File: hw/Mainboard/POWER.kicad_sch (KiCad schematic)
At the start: 36 parts, among them J10 5V PWR, J11 3V3 PWR, J18 PET_Power_01x09_Male, J7 9V POWER, U10 XL1509-5.0E1, U15 LM317AG-TN3-R

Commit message: hw: wip add MCU, 2 layer board
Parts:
- removed D8: YLW LED, LED_SMD:LED_0603_1608Metric, symbol Device:LED
- removed D9: GRN LED, LED_SMD:LED_0603_1608Metric, symbol Device:LED
- removed J11: 3V3 PWR, Connector_PinHeader_2.54mm:PinHeader_1x03_P2.54mm_Vertical, symbol Connector:Conn_01x03_Male
- removed R48: 1.5k, Resistor_SMD:R_0402_1005Metric, symbol Device:R_Small
- removed R51: 1k, Resistor_SMD:R_0402_1005Metric, symbol Device:R_Small
- added C21: 22u 25V, Capacitor_SMD:C_0805_2012Metric, symbol Device:C_Small
- added C34: 10uF 50V, Capacitor_SMD:C_1206_3216Metric, symbol Device:C_Small
- added C36: 22u, Capacitor_SMD:C_0805_2012Metric, symbol Device:C_Small
- added H3, H4: MountingHole, PET:PET_MountingHole_4mm, symbol Mechanical:MountingHole
- added U13: AMS1117-3.3, Package_TO_SOT_SMD:SOT-223-3_TabPin2, symbol Regulator_Linear:AMS1117-3.3
- C29: value 1u -> 1u 25V
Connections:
- net +3V3: now also C36.1, U13.2 (VO)
- net +5V: now also C21.1, C34.1, U13.3 (VI)
- net GND: now also C21.2, C34.2, C36.2, U13.1 (GND)
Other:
- moved on the sheet: C14, C16, C22, C26, C29, C32, H1, H2, R42, R43, R45, R46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

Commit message: hw: T8 (wip)
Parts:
- added C52, C53: 22u 25V, Capacitor_SMD:C_0805_2012Metric, symbol Device:C_Small
- added C54, C55: 10u, Capacitor_Tantalum_SMD:CP_EIA-3216-18_Kemet-A, symbol T8Dev-rescue:CP-Device
- added C56, C57: 100n, Capacitor_SMD:C_0402_1005Metric, symbol Device:C_Small
- added C58: 4.7u, Capacitor_SMD:C_0402_1005Metric, symbol Device:C_Small
- added FB1: 600, Inductor_SMD:L_0603_1608Metric, symbol T8Dev-rescue:Ferrite_Bead_Small-Device
- added U17: LM1117-1.2, Package_TO_SOT_SMD:SOT-223, symbol Regulator_Linear:LM1117-3.3
- added U21: T8Q144C3, SnapEDA:QFP50P2200X2200X160-144N, symbol SnapEDA:T8Q144C3
- J18: value PET_Power_01x09_Male -> PET POWER
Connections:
- net +3V3: now also C54.1, U17.3 (VI), U21.12 (VCCIO1C_1D), U21.122 (VCCIO3A), U21.143 (VCCIO1E), U21.21 (VCCIO1B), U21.23 (VCCIO1A), U21.51 (VCCIO4B), U21.52 (VCCIO4B), U21.62 (VCCIO4A), U21.63 (VCCIO4A), U21.88 (VCCIO3E), U21.91 (VCCIO3D), U21.95 (VCCIO3B_3C)
- net +9V_Unreg: now also C52.1, C53.1; no longer C13.1
- net GND: now also C52.2, C53.2, C54.2, C55.2, C56.2, C57.2, C58.2, U17.1 (GND), U21.1 (GND), U21.104 (GND), U21.108 (GND), U21.120 (GND), U21.121 (GND), U21.126 (GND), U21.127 (GND), U21.129 (GND), U21.133 (GND), U21.37 (GND), U21.44 (GND), U21.5 (GND), U21.50 (GND), U21.64 (GND), U21.9 (GND), U21.94 (GND)
- net at C12.2, C15.1, C33.2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: now also C13.1
- new net: C57.1, C58.1, FB1.1, U21.107 (VCCA_TR), U21.2 (VCCA_TL), U21.73 (VCCA_BR)
- new net VCORE: C55.1, C56.1, FB1.2, U17.2 (VO), U21.125 (VCC), U21.128 (VCC), U21.13 (VCC), U21.130 (VCC), U21.22 (VCC), U21.49 (VCC), U21.57 (VCC), U21.85 (VCC), U21.96 (VCC)
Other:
- note added: "Dropout Voltage = 1.3V"
- note added: "T8Q144 Power Requirements Absolute max VCORE: 1.42V Typical: 1.15V ~ 1.25V"
- note added: "VCCA is the analog VCORE source for PLLs"
- moved on the sheet: C12, C13, C14, C15, C16, C17, C21, C22, C26, C29, C32, C33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

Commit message: hw: routing (excluding MCU)
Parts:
- added J11: 9V POWER, Connector_PinHeader_2.54mm:PinHeader_1x02_P2.54mm_Vertical, symbol Connector:Conn_01x02_Male
- C36: value 22u -> 22u 25V
- C54, C55: value 10u -> 10u 16V
- D1: value RED LED -> RED_9V
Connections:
- net +9V_Unreg: now also J11.2 (Pin_2)
- net GND: now also J11.1 (Pin_1)
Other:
- note added: "AMS1117-3.3: Dropout Voltage = 1.3V"
- note added: "T8Q144 Power Requirements Absolute max VCORE: 1.42V Typical: 1.15V ~ 1.25V LM1117-12: VOUT = 1.176V - 1.224V (IOUT = 10ma, VIN = 3.5V) VOUT = 1.152V - 1.248V (10mA <= IOUT <= 1A, 3.0 <= VIN <= 10V) VIN = 12V (max recommended) Dropout Voltage = 1.2V @ 1A"
- note removed: "Dropout Voltage = 1.3V"
- note removed: "T8Q144 Power Requirements Absolute max VCORE: 1.42V Typical: 1.15V ~ 1.25V"
- moved on the sheet: C55
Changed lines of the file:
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@@
   (junction (at 242.57 144.78) (diameter 0) (color 0 0 0 0)
   )
+  (junction (at 54.61 38.1) (diameter 0) (color 0 0 0 0)
+  )
   (junction (at 109.22 106.68) (diameter 0) (color 0 0 0 0)
   )
@@
   (junction (at 147.32 49.53) (diameter 0) (color 0 0 0 0)
   )
+  (junction (at 45.72 43.18) (diameter 0) (color 0 0 0 0)
+  )
   (junction (at 109.22 68.58) (diameter 0) (color 0 0 0 0)
   )
@@
   (junction (at 172.72 49.53) (diameter 0) (color 0 0 0 0)
   )
-  (junction (at 142.24 135.89) (diameter 0) (color 0 0 0 0)
-  )
   (junction (at 186.69 49.53) (diameter 0) (color 0 0 0 0)
   )
@@
   )
   (junction (at 242.57 119.38) (diameter 0) (color 0 0 0 0)
+  )
+  (junction (at 144.78 135.89) (diameter 0) (color 0 0 0 0)
   )
   (junction (at 241.3 111.76) (diameter 0) (color 0 0 0 0)
@@
     (stroke (width 0) (type default) (color 0 0 0 0))
   )
-  (wire (pts (xy 142.24 144.78) (xy 128.27 144.78))
+  (wire (pts (xy 128.27 144.78) (xy 144.78 144.78))
     (stroke (width 0) (type default) (color 0 0 0 0))
   )
@@
     (stroke (width 0) (type default) (color 0 0 0 0))
   )
+  (wire (pts (xy 54.61 38.1) (xy 67.31 38.1))
+    (stroke (width 0) (type default) (color 0 0 0 0))
+  )
   (wire (pts (xy 39.37 40.64) (xy 39.37 43.18))
     (stroke (width 0) (type default) (color 0 0 0 0))
@@
     (stroke (width 0) (type default) (color 0 0 0 0))
   )
-  (wire (pts (xy 142.24 135.89) (xy 157.48 135.89))
+  (wire (pts (xy 135.89 135.89) (xy 144.78 135.89))
     (stroke (width 0) (type default) (color 0 0 0 0))
   )
@@
     (stroke (width 0) (type default) (color 0 0 0 0))
   )
+  (wire (pts (xy 45.72 43.18) (xy 67.31 43.18))
+    (stroke (width 0) (type default) (color 0 0 0 0))
+  )
   (wire (pts (xy 243.84 119.38) (xy 242.57 119.38))
     (stroke (width 0) (type default) (color 0 0 0 0))
@@
     (stroke (width 0) (type default) (color 0 0 0 0))
   )
-  (wire (pts (xy 142.24 143.51) (xy 142.24 144.78))
+  (wire (pts (xy 144.78 143.51) (xy 144.78 144.78))
     (stroke (width 0) (type default) (color 0 0 0 0))
   )
@@
     (stroke (width 0) (type default) (color 0 0 0 0))
   )
-  (wire (pts (xy 135.89 135.89) (xy 142.24 135.89))
-    (stroke (width 0) (type default) (color 0 0 0 0))
-  )
   (wire (pts (xy 259.08 31.75) (xy 255.27 31.75))
     (stroke (width 0) (type default) (color 0 0 0 0))
@@
     (stroke (width 0) (type default) (color 0 0 0 0))
   )
+  (wire (pts (xy 144.78 135.89) (xy 157.48 135.89))
+    (stroke (width 0) (type default) (color 0 0 0 0))
+  )
   (wire (pts (xy 246.38 50.8) (xy 247.65 50.8))
     (stroke (width 0) (type default) (color 0 0 0 0))
@@
     (stroke (width 0) (type default) (color 0 0 0 0))
   )
+  (wire (pts (xy 67.31 40.64) (xy 67.31 43.18))
+    (stroke (width 0) (type default) (color 0 0 0 0))
+  )
   (wire (pts (xy 27.94 93.98) (xy 36.83 93.98))
     (stroke (width 0) (type default) (color 0 0 0 0))
@@
     (stroke (width 0) (type default) (color 0 0 0 0))
   )
-  (text "T8Q144 Power Requirements\n\nAbsolute max VCORE: 1.42V\nTypical: 1.15V ~ 1.25V"
-    (at 134.62 156.21 0)
+  (text "T8Q144 Power Requirements\nAbsolute max VCORE: 1.42V\nTypical: 1.15V ~ 1.25V\n\nLM1117-12:\nVOUT = 1.176V - 1.224V (IOUT = 10ma, VIN = 3.5V)\nVOUT = 1.152V - 1.248V (10mA <= IOUT <= 1A, 3.0 <= VIN <= 10V)\nVIN = 12V (max recommended)\nDropout Voltage = 1.2V @ 1A"
+    (at 166.37 146.05 0)
     (effects (font (size 1.27 1.27)) (justify left bottom))
   )
   (text "In the PET, pins 2 and 4 are connected externally with a\n23000u capacitor to reduce ripple in the rectified 9V.\n\nOlder 2001 PETs had a 5 pin connector, which was expanded\nto 9 pins in a compatible way.  Pin 7 is key.  Pins 8/9\nare an additional AC input for generating +16V and +12V.\n\nRAW power connectors shown in the original PET schematics\nprovide unregulated +16V/-9V power to internal accessories,\nsuch as RAM expanders.\n\nThe PET monitor gets power directly from the transformer.\n"
-    (at 22.86 144.78 0)
+    (at 20.32 147.32 0)
     (effects (font (size 1.27 1.27)) (justify left bottom))
   )
@@
     (effects (font (size 1.27 1.27)) (justify left bottom))
   )
-  (text "Dropout Voltage = 1.3V" (at 135.89 120.65 0)
+  (text "AMS1117-3.3:\nDropout Voltage = 1.3V" (at 138.43 123.19 0)
     (effects (font (size 1.27 1.27)) (justify left bottom))
   )
@@
     (in_bom yes) (on_board yes)
     (property "Reference" "D1" (id 0) (at 263.0678 25.273 0))
-    (property "Value" "RED LED" (id 1) (at 263.0678 27.5844 0))
+    (property "Value" "RED_9V" (id 1) (at 263.0678 27.5844 0))
     (property "Footprint" "LED_SMD:LED_0603_1608Metric" (id 2) (at 262.89 31.75 0)
       (effects (font (size 1.27 1.27)) hide)
@@
     )
     (pin "1")
+  )
+  (symbol (lib_id "Connector:Conn_01x02_Male") (at 72.39 40.64 180) (unit 1)
+    (in_bom yes) (on_board yes) (fields_autoplaced)
+    (property "Reference" "J11" (id 0) (at 73.66 38.0999 0)
+      (effects (font (size 1.27 1.27)) (justify right))
+    )
+    (property "Value" "9V POWER" (id 1) (at 73.66 40.6399 0)
+      (effects (font (size 1.27 1.27)) (justify right))
+    )
+    (property "Footprint" "Connector_PinHeader_2.54mm:PinHeader_1x02_P2.54mm_Vertical" (id 2) (at 72.39 40.64 0)
+      (effects (font (size 1.27 1.27)) hide)
+    )
+    (property "Datasheet" "~" (id 3) (at 72.39 40.64 0)
+      (effects (font (size 1.27 1.27)) hide)
+    )
+    (pin "1")
+    (pin "2")
   )
   (symbol (lib_id "SnapEDA:T8Q144C3") (at 259.08 127 0) (unit 13)
@@
       (effects (font (size 1.27 1.27)) (justify left))
     )
-    (property "Value" "22u" (id 1) (at 147.32 111.7662 0)
+    (property "Value" "22u 25V" (id 1) (at 147.32 111.7662 0)
       (effects (font (size 1.27 1.27)) (justify left))
     )
@@
       (effects (font (size 1.27 1.27)) (justify left))
     )
-    (property "Value" "10u" (id 1) (at 112.2172 140.843 0)
+    (property "Value" "10u 16V" (id 1) (at 112.2172 140.843 0)
       (effects (font (size 1.27 1.27)) (justify left))
     )
@@
     (pin "1")
   )
-  (symbol (lib_id "T8Dev-rescue:CP-Device") (at 142.24 139.7 0) (unit 1)
-    (in_bom yes) (on_board yes)
-    (property "Reference" "C55" (id 0) (at 145.2372 138.5316 0)
-      (effects (font (size 1.27 1.27)) (justify left))
-    )
-    (property "Value" "10u" (id 1) (at 145.2372 140.843 0)
-      (effects (font (size 1.27 1.27)) (justify left))
-    )
-    (property "Footprint" "Capacitor_Tantalum_SMD:CP_EIA-3216-18_Kemet-A" (id 2) (at 143.2052 143.51 0)
-      (effects (font (size 1.27 1.27)) hide)
-    )
-    (property "Datasheet" "https://datasheet.lcsc.com/lcsc/1811071223_AVX-TAJA106K016RNJ_C7171.pdf" (id 3) (at 142.24 139.7 0)
-      (effects (font (size 1.27 1.27)) hide)
-    )
-    (property "LCSC" "C7171" (id 4) (at 142.24 139.7 0)
-      (effects (font (size 1.27 1.27)) hide)
-    )
+  (symbol (lib_id "T8Dev-rescue:CP-Device") (at 144.78 139.7 0) (unit 1)
+    (in_bom yes) (on_board yes)
+    (property "Reference" "C55" (id 0) (at 147.7772 138.5316 0)
+      (effects (font (size 1.27 1.27)) (justify left))
+    )
+    (property "Value" "10u 16V" (id 1) (at 147.7772 140.843 0)
+      (effects (font (size 1.27 1.27)) (justify left))
+    )
+    (property "Footprint" "Capacitor_Tantalum_SMD:CP_EIA-3216-18_Kemet-A" (id 2) (at 145.7452 143.51 0)
+      (effects (font (size 1.27 1.27)) hide)
+    )
+    (property "Datasheet" "https://datasheet.lcsc.com/lcsc/1811071223_AVX-TAJA106K016RNJ_C7171.pdf" (id 3) (at 144.78 139.7 0)
+      (effects (font (size 1.27 1.27)) hide)
+    )
+    (property "LCSC" "C7171" (id 4) (at 144.78 139.7 0)
+      (effects (font (size 1.27 1.27)) hide)
+    )

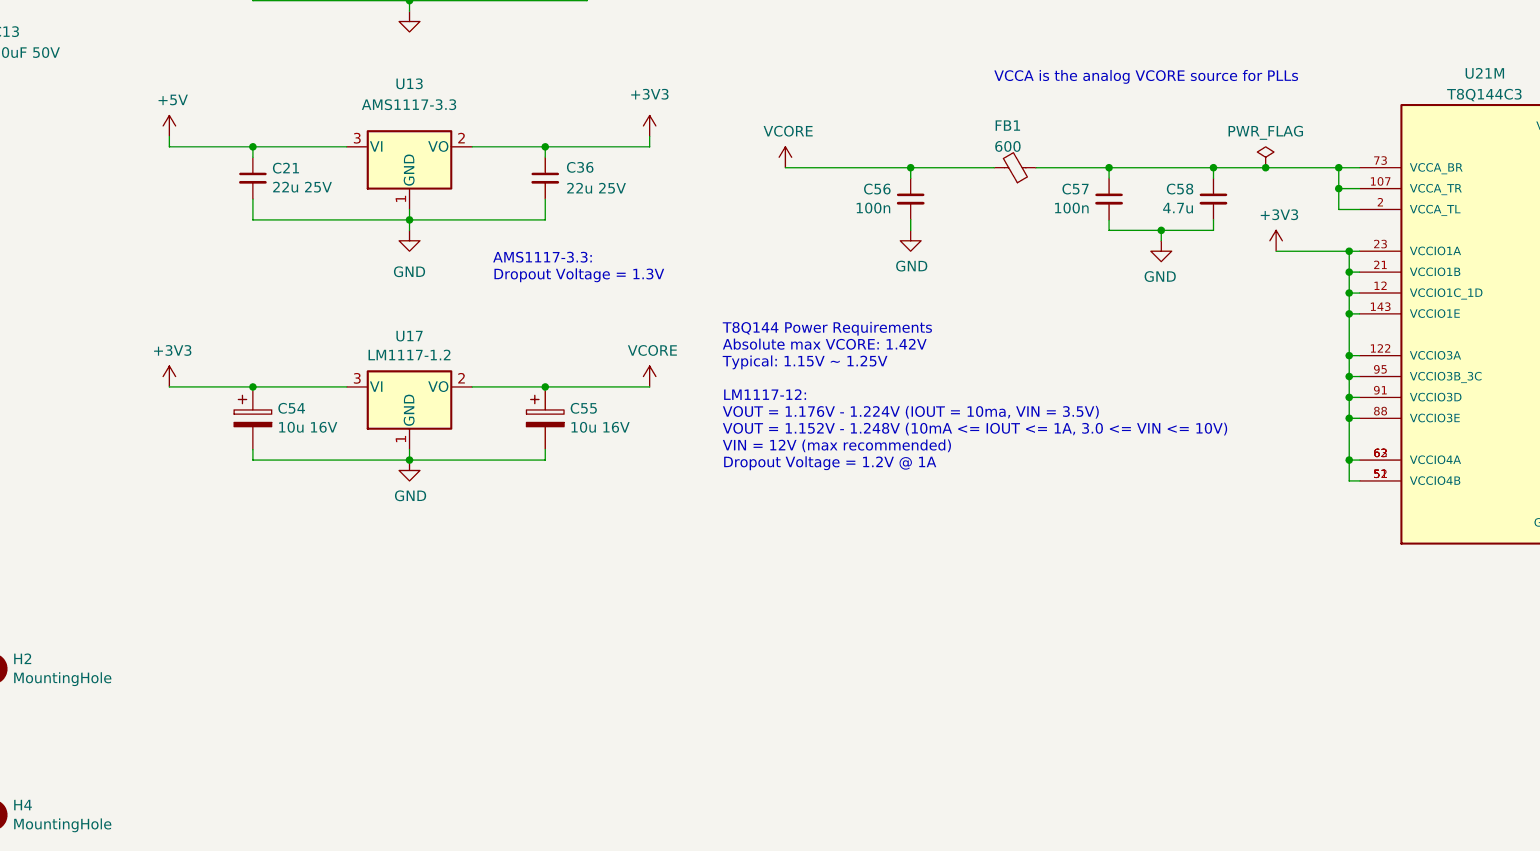
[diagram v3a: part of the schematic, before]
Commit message: hw: routed, but trace sizes need to be reviewed/fixed
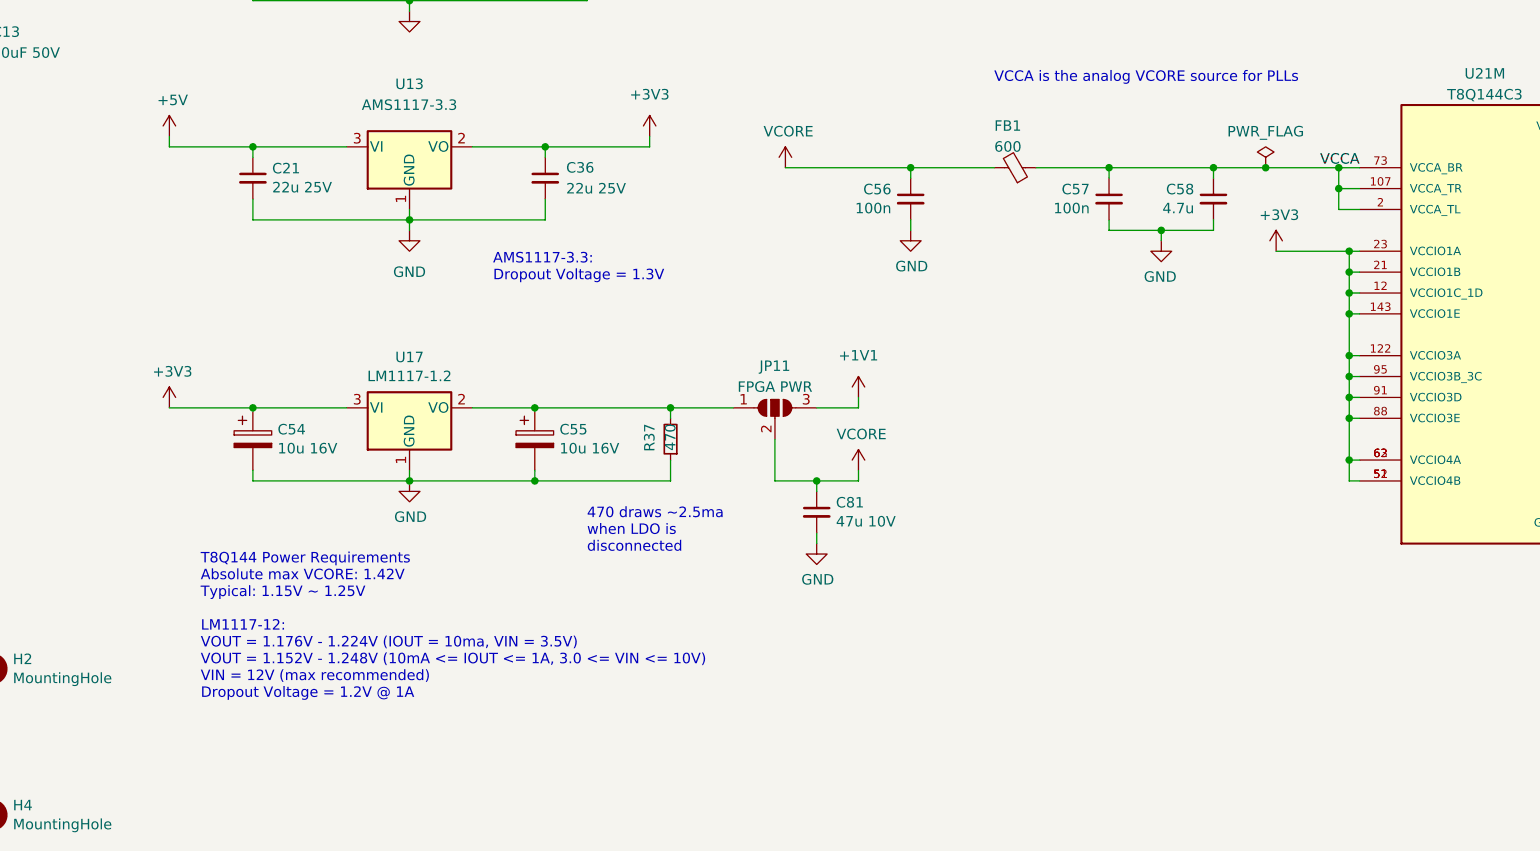
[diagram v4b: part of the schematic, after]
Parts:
- added C81: 47u 10V, Capacitor_SMD:C_1206_3216Metric, symbol Device:C_Small
- added JP11: FPGA PWR, Jumper:SolderJumper-3_P1.3mm_Bridged12_RoundedPad1.0x1.5mm, symbol Jumper:SolderJumper_3_Open
- added R37: 470, Resistor_SMD:R_0402_1005Metric, symbol Device:R_Small
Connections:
- net GND: now also C81.2, R37.1
- net VCORE: now also C81.1, JP11.2 (C); no longer C55.1, U17.2 (VO)
- net VCCA: now reaches C57.1, C58.1, FB1.1, U21.107 (VCCA_TR), U21.2 (VCCA_TL), U21.73 (VCCA_BR)
- new net: C55.1, JP11.1 (A), R37.2, U17.2 (VO)
- new net +1V1: JP11.3 (B)
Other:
- note added: "470 draws ~2.5ma when LDO is disconnected"
- moved on the sheet: C54, C55, U17

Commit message: hw: routable (wip)
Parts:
- removed U21: T8Q144C3, SnapEDA:QFP50P2200X2200X160-144N, symbol SnapEDA:T8Q144C3
- added NT1, NT17: GND, PET:NetTie-2_SMD_Pad_1.6_to_0.4mm, symbol Device:NetTie_2
- added NT16, NT2: +9V, PET:NetTie-2_SMD_Pad_1.6_to_0.4mm, symbol Device:NetTie_2
- C35: footprint Capacitor_THT:CP_Radial_D10.0mm_P5.00mm -> PET:CP_Radial_D16.0mm_P5.00mm_P7.50mm
- JP11: value FPGA PWR -> FPGA VCC
- R41: value 2.7k -> 2k7
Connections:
- net +9V_Unreg: now also NT2.1; no longer C17.1, U10.1 (Input)
- net GND: no longer C13.2, C14.2, C16.2, C17.2, C26.2, C32.2, C33.1, C34.2, C35.2, C52.2, C53.2, D2.2 (A), D5.2 (A), J11.1 (Pin_1), J18.3 (Pin_3), J18.6 (Pin_6), J7.2, J7.3, R42.2, U10.4 (~{EN}), U10.5 (GND), U10.6 (GND), U10.7 (GND), U10.8 (GND)
- net +1V1 renamed MCU_DVDD
- net +5V renamed PD_5V
- net PD_5V: now also NT17.1; no longer U10.3 (FB)
- net +6V: no longer names the net of C29.1, R43.1, R47.1
- net +6V: now also NT16.2; no longer U15.2 (VO)
- net GNDPWR renamed CHASSIS_GND
- net VCCA renamed FPGA_VCCA
- net VCORE renamed FPGA_VCC
- new net: C17.1, NT2.2, U10.1 (Input)
- new net: C17.2, NT1.2
- new net: NT17.2, U10.3 (FB)
- new net PD_6V: NT16.1, U15.2 (VO)
- new net PD_GND: C13.2, C14.2, C16.2, C26.2, C32.2, C33.1, C34.2, C35.2, C52.2, C53.2, D2.2 (A), D5.2 (A), J11.1 (Pin_1), J18.3 (Pin_3), J18.6 (Pin_6), J7.2, J7.3, NT1.1, R42.2, U10.4 (~{EN}), U10.5 (GND), U10.6 (GND), U10.7 (GND), U10.8 (GND)
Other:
- note added: "VOUT=1.25V×(1+R2/R1) 6.1V @ 400ma typical / 700ma max (350ma per cassette port) Voltage and limits derived from PET schematics and datasheets"
- note removed: "6.1V @ 400ma typical / 700ma max (350ma per cassette port) Voltage and limits derived from PET schematics and datasheets"
- note removed: "VOUT=1.25V×(1+R2/R1)"
- moved on the sheet: C29, C56, C57, C58, FB1, R42, R43, R47
